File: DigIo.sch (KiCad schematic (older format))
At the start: 2 parts

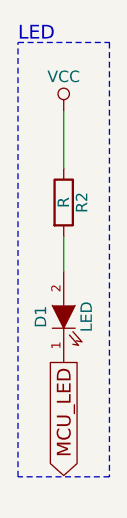
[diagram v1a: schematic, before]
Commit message: Update schematic and reroute print
 * Update opamp circuit for light sensor
 * Change opamp
 * Reroute everything

Signed-off-by: Philip Luyckx <philip.luyckx@gmail.com>
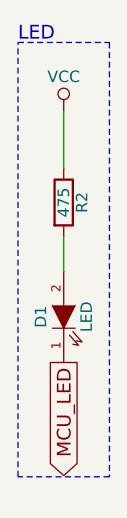
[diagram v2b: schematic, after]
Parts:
- R2: value R -> 475
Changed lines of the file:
@@
 P 4300 3000
 F 0 "R2" V 4380 3000 50  0000 C CNN
-F 1 "R" V 4300 3000 50  0000 C CNN
+F 1 "475" V 4300 3000 50  0000 C CNN
 F 2 "Resistors_SMD:R_1206" V 4230 3000 30  0001 C CNN
 F 3 "" H 4300 3000 30  0000 C CNN
@@
 $EndComp
 $Comp
-L VCC #PWR17
+L VCC #PWR017
 U 1 1 566214F9
 P 4300 2600
-F 0 "#PWR17" H 4300 2450 50  0001 C CNN
+F 0 "#PWR017" H 4300 2450 50  0001 C CNN
 F 1 "VCC" H 4300 2750 50  0000 C CNN
 F 2 "" H 4300 2600 60  0000 C CNN

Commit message: Use 0603 resistors
Signed-off-by: Philip Luyckx <philip.luyckx@gmail.com>
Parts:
- R2: footprint Resistors_SMD:R_1206 -> Resistors_SMD:R_0603
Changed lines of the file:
@@
 F 0 "R2" V 4380 3000 50  0000 C CNN
 F 1 "475" V 4300 3000 50  0000 C CNN
-F 2 "Resistors_SMD:R_1206" V 4230 3000 30  0001 C CNN
+F 2 "Resistors_SMD:R_0603" V 4230 3000 30  0001 C CNN
 F 3 "" H 4300 3000 30  0000 C CNN
 	1    4300 3000

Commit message: Finish work on V2
 * Rework layout
 * Reassign mcu pins
 * Add a capacitor for the RF module

Signed-off-by: Philip Luyckx <philip.luyckx@gmail.com>
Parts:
- D1: footprint CustomSmd:R_ThroughHole_SMD1206 -> Resistors_SMD:R_1206
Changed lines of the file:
@@
 F 0 "D1" H 4300 3600 50  0000 C CNN
 F 1 "LED" H 4300 3400 50  0000 C CNN
-F 2 "CustomSmd:R_ThroughHole_SMD1206" H 4300 3500 60  0001 C CNN
+F 2 "Resistors_SMD:R_1206" H 4300 3500 60  0001 C CNN
 F 3 "" H 4300 3500 60  0000 C CNN
 	1    4300 3500
@@
 $EndComp
 $Comp
-L VCC #PWR017
+L VCC #PWR016
 U 1 1 566214F9
 P 4300 2600
-F 0 "#PWR017" H 4300 2450 50  0001 C CNN
+F 0 "#PWR016" H 4300 2450 50  0001 C CNN
 F 1 "VCC" H 4300 2750 50  0000 C CNN
 F 2 "" H 4300 2600 60  0000 C CNN
